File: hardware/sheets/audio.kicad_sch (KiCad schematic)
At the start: 17 parts, among them J2 LineOut_TRS, U1 MCP6002

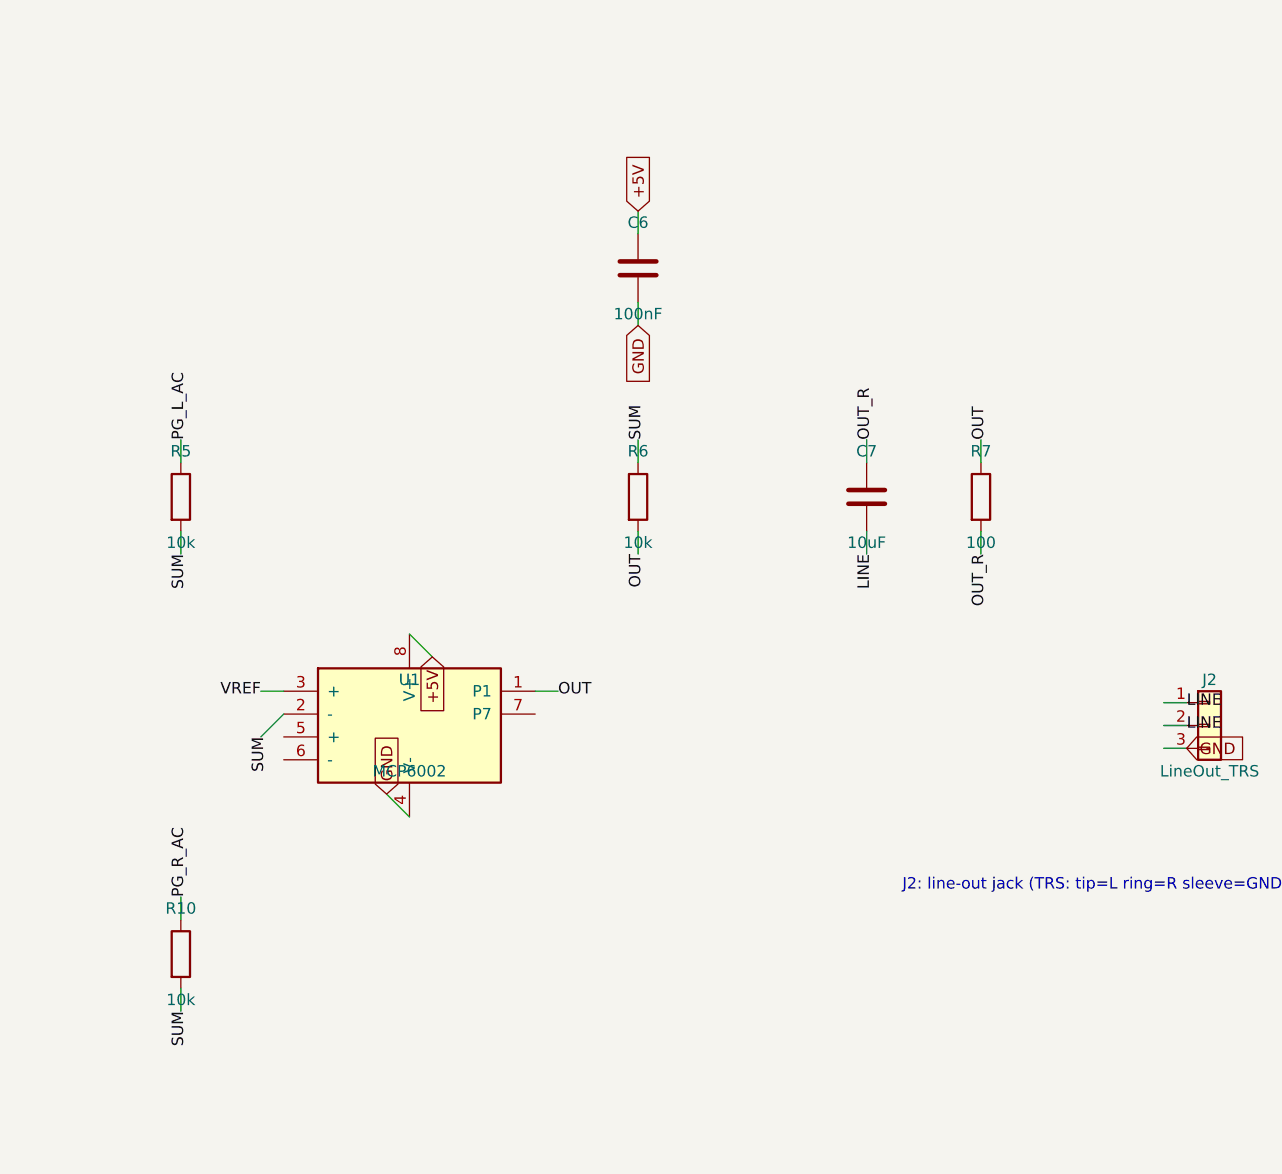
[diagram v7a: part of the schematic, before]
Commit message: Design-review fixes: reset parking, IRQ8 off the header, analog cleanups
Netlist-wide review sweep. IRQ8 leaves the 60-pin ISA header (pin 15 is a
second GND return; the on-board RTC owns IRQ8 exclusively, so its push-pull
drive is now correct by construction). Bus MCU Hi-Z parking completed:
~CPURESET pulled low (V20 held in reset while the MCU is unprogrammed),
~DACK1/~REFRESH parked deasserted, DRQ1 idled low. Supervisor 12 MHz crystal
damping R actually in series now (was parallel-to-nothing), plus a second
USBLC6 so both prog-port SW2 positions are ESD-protected. Audio: 0.5x PG
summing (MCP6002 headroom), 100k LINE bleed, unit B parked as a follower --
and the SUM stub moved off pin 5's row, where wiring unit B would have
silently merged SUM into VREF. CH224K VDD fed through 1k per the WCH ref
design. VGA blue ladder rescaled 1k/510 -> 820/470 (was ~12% blue-deficient).
Spare CMOS gate inputs grounded uniformly (cpu_core/rtc/storage); UART_RXD
pulled up (SIN idles at mark with JP1 open); dead pins/parts dropped
(com_port CLK, parallel RESET_DRV, storage R3). Bus CLK fixed at 7.16 MHz
logged as a decision. New passives mapped to JLC basic parts in parts.py.

Co-Authored-By: Claude Fable 5 <noreply@anthropic.com>
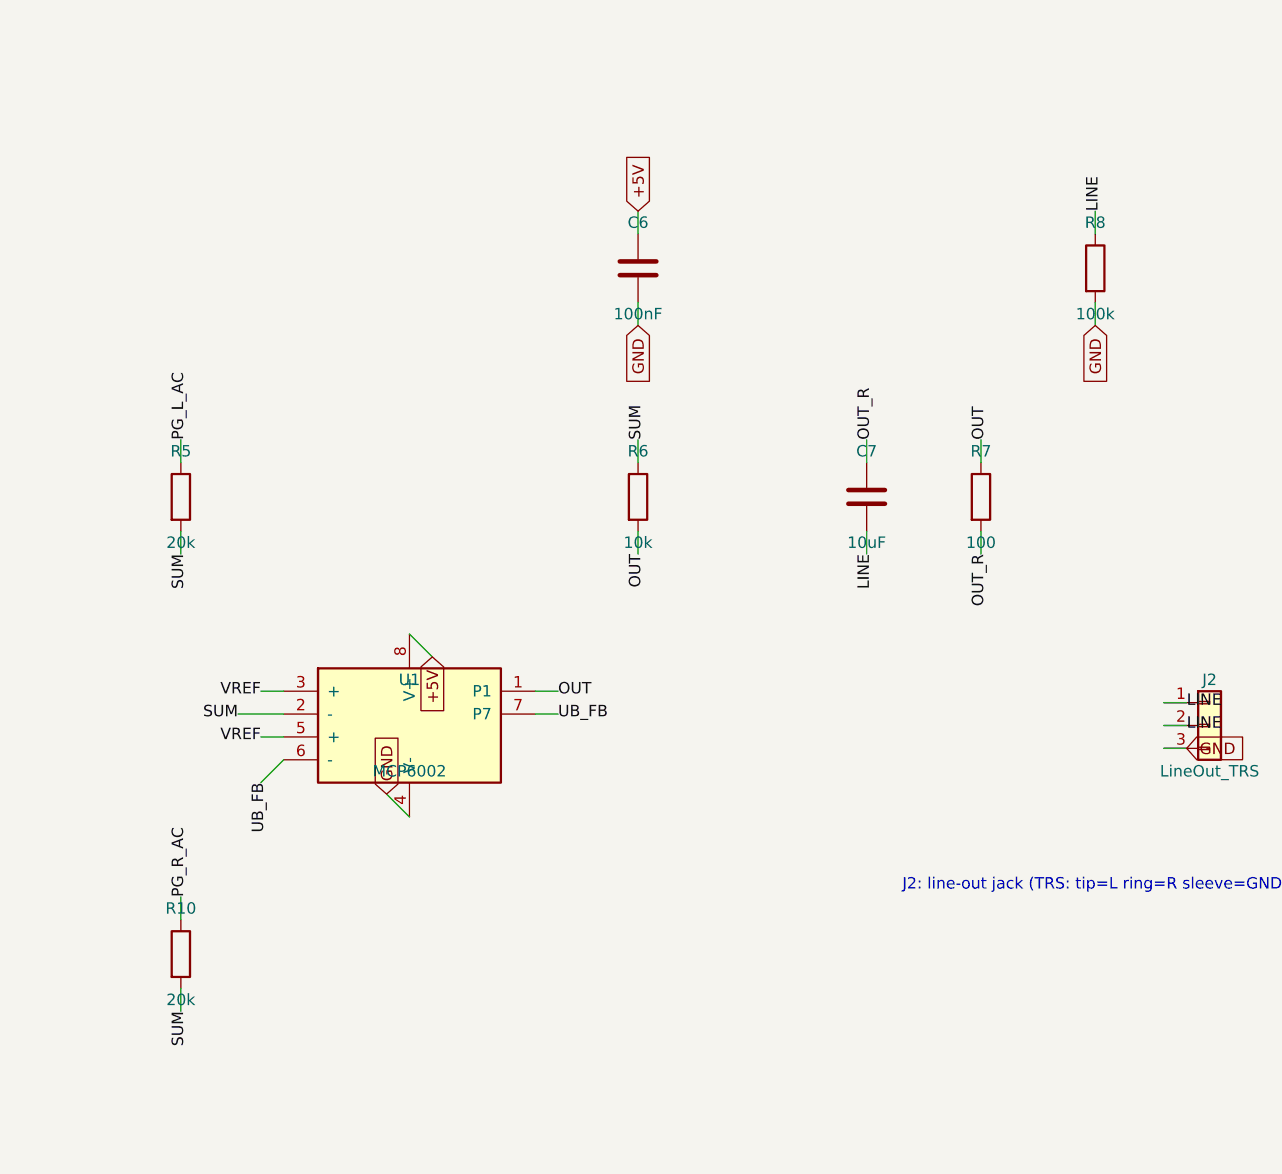
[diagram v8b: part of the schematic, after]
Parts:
- added J2: LineOut_TRS, symbol Connector_Generic:Conn_01x03
- R10, R5: value 10k -> 20k; LCSC Part Num C25804 -> C4184
- R8: renamed from J2; value LineOut_TRS -> 100k; symbol Connector_Generic:Conn_01x03 -> Device:R; LCSC Part Num C2337 -> C25803
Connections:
- net GND: now also R8.2, J2.3 (Pin_3); no longer R8.3 (Pin_3)
- net LINE: now also J2.1 (Pin_1), J2.2 (Pin_2); no longer R8.2 (Pin_2)
- net VREF: now also U1.5 (+)
- net UB_FB: now reaches U1.6 (-)
- net UB_FB: now also U1.7 (P7)
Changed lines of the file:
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@@
 		(pts
 			(xy 163.83 151.13)
-			(xy 161.29 153.67)
+			(xy 158.75 151.13)
 		)
 		(stroke
@@
 	)
 	(label "SUM"
-		(at 161.29 153.67 270)
+		(at 158.75 151.13 180)
 		(effects
 			(font
@@
 	(label "LINE"
 		(at 228.6 133.35 270)
+		(effects
+			(font
+				(size 1.27 1.27)
+			)
+		)
+	)
+	(wire
+		(pts
+			(xy 254 97.79)
+			(xy 254 95.25)
+		)
+		(stroke
+			(width 0)
+			(type default)
+		)
+	)
+	(label "LINE"
+		(at 254 95.25 90)
+		(effects
+			(font
+				(size 1.27 1.27)
+			)
+		)
+	)
+	(wire
+		(pts
+			(xy 254 105.41)
+			(xy 254 107.95)
+		)
+		(stroke
+			(width 0)
+			(type default)
+		)
+	)
+	(global_label "GND"
+		(shape input)
+		(at 254 107.95 270)
+		(effects
+			(font
+				(size 1.27 1.27)
+			)
+		)
+	)
+	(wire
+		(pts
+			(xy 163.83 153.67)
+			(xy 161.29 153.67)
+		)
+		(stroke
+			(width 0)
+			(type default)
+		)
+	)
+	(label "VREF"
+		(at 161.29 153.67 180)
+		(effects
+			(font
+				(size 1.27 1.27)
+			)
+		)
+	)
+	(wire
+		(pts
+			(xy 163.83 156.21)
+			(xy 161.29 158.75)
+		)
+		(stroke
+			(width 0)
+			(type default)
+		)
+	)
+	(label "UB_FB"
+		(at 161.29 158.75 270)
+		(effects
+			(font
+				(size 1.27 1.27)
+			)
+		)
+	)
+	(wire
+		(pts
+			(xy 191.77 151.13)
+			(xy 194.31 151.13)
+		)
+		(stroke
+			(width 0)
+			(type default)
+		)
+	)
+	(label "UB_FB"
+		(at 194.31 151.13 0)
 		(effects
 			(font
@@
 		(instances
 			(project "mini-xt"
-				(path "/26736c46-8b40-5460-874f-03596d17270c/3608bfd0-7703-513a-bc2e-2c197268d7ed"
+				(path "/26736c46-8b40-5460-874f-03596d17270c/4d185cde-1239-5609-9fdc-bfd3b5da75e8"
 					(reference "R1101")
 					(unit 1)
@@
 		(instances
 			(project "mini-xt"
-				(path "/26736c46-8b40-5460-874f-03596d17270c/3608bfd0-7703-513a-bc2e-2c197268d7ed"
+				(path "/26736c46-8b40-5460-874f-03596d17270c/4d185cde-1239-5609-9fdc-bfd3b5da75e8"
 					(reference "R1102")
 					(unit 1)
@@
 		(instances
 			(project "mini-xt"
-				(path "/26736c46-8b40-5460-874f-03596d17270c/3608bfd0-7703-513a-bc2e-2c197268d7ed"
+				(path "/26736c46-8b40-5460-874f-03596d17270c/4d185cde-1239-5609-9fdc-bfd3b5da75e8"
 					(reference "C1101")
 					(unit 1)
@@
 		(instances
 			(project "mini-xt"
-				(path "/26736c46-8b40-5460-874f-03596d17270c/3608bfd0-7703-513a-bc2e-2c197268d7ed"
+				(path "/26736c46-8b40-5460-874f-03596d17270c/4d185cde-1239-5609-9fdc-bfd3b5da75e8"
 					(reference "R1103")
 					(unit 1)
@@
 		(instances
 			(project "mini-xt"
-				(path "/26736c46-8b40-5460-874f-03596d17270c/3608bfd0-7703-513a-bc2e-2c197268d7ed"
+				(path "/26736c46-8b40-5460-874f-03596d17270c/4d185cde-1239-5609-9fdc-bfd3b5da75e8"
 					(reference "C1102")
 					(unit 1)
@@
 		(instances
 			(project "mini-xt"
-				(path "/26736c46-8b40-5460-874f-03596d17270c/3608bfd0-7703-513a-bc2e-2c197268d7ed"
+				(path "/26736c46-8b40-5460-874f-03596d17270c/4d185cde-1239-5609-9fdc-bfd3b5da75e8"
 					(reference "C1103")
 					(unit 1)
@@
 		(instances
 			(project "mini-xt"
-				(path "/26736c46-8b40-5460-874f-03596d17270c/3608bfd0-7703-513a-bc2e-2c197268d7ed"
+				(path "/26736c46-8b40-5460-874f-03596d17270c/4d185cde-1239-5609-9fdc-bfd3b5da75e8"
 					(reference "C1104")
 					(unit 1)
@@
 		(instances
 			(project "mini-xt"
-				(path "/26736c46-8b40-5460-874f-03596d17270c/3608bfd0-7703-513a-bc2e-2c197268d7ed"
+				(path "/26736c46-8b40-5460-874f-03596d17270c/4d185cde-1239-5609-9fdc-bfd3b5da75e8"
 					(reference "C1105")
 					(unit 1)
@@
 		(instances
 			(project "mini-xt"
-				(path "/26736c46-8b40-5460-874f-03596d17270c/3608bfd0-7703-513a-bc2e-2c197268d7ed"
+				(path "/26736c46-8b40-5460-874f-03596d17270c/4d185cde-1239-5609-9fdc-bfd3b5da75e8"
 					(reference "U1101")
 					(unit 1)
@@
 		(instances
 			(project "mini-xt"
-				(path "/26736c46-8b40-5460-874f-03596d17270c/3608bfd0-7703-513a-bc2e-2c197268d7ed"
+				(path "/26736c46-8b40-5460-874f-03596d17270c/4d185cde-1239-5609-9fdc-bfd3b5da75e8"
 					(reference "C1106")
 					(unit 1)
@@
 		(instances
 			(project "mini-xt"
-				(path "/26736c46-8b40-5460-874f-03596d17270c/3608bfd0-7703-513a-bc2e-2c197268d7ed"
+				(path "/26736c46-8b40-5460-874f-03596d17270c/4d185cde-1239-5609-9fdc-bfd3b5da75e8"
 					(reference "R1104")
 					(unit 1)
@@
 			)
 		)
-		(property "Value" "10k"
+		(property "Value" "20k"
 			(at 152.4 132.08 0)
 			(effects
@@
 			)
 		)
-		(property "LCSC Part Num" "C25804"
+		(property "LCSC Part Num" "C4184"
 			(at 152.4 127 0)
 			(effects
@@
 		(instances
 			(project "mini-xt"
-				(path "/26736c46-8b40-5460-874f-03596d17270c/3608bfd0-7703-513a-bc2e-2c197268d7ed"
+				(path "/26736c46-8b40-5460-874f-03596d17270c/4d185cde-1239-5609-9fdc-bfd3b5da75e8"
 					(reference "R1105")
 					(unit 1)
@@
 			)
 		)
-		(property "Value" "10k"
+		(property "Value" "20k"
 			(at 152.4 182.88 0)
 			(effects
@@
 			)
 		)
-		(property "LCSC Part Num" "C25804"
+		(property "LCSC Part Num" "C4184"
 			(at 152.4 177.8 0)
 			(effects
@@
 		(instances
 			(project "mini-xt"
-				(path "/26736c46-8b40-5460-874f-03596d17270c/3608bfd0-7703-513a-bc2e-2c197268d7ed"
+				(path "/26736c46-8b40-5460-874f-03596d17270c/4d185cde-1239-5609-9fdc-bfd3b5da75e8"
 					(reference "R1110")
 					(unit 1)
@@
 		(instances
 			(project "mini-xt"
-				(path "/26736c46-8b40-5460-874f-03596d17270c/3608bfd0-7703-513a-bc2e-2c197268d7ed"
+				(path "/26736c46-8b40-5460-874f-03596d17270c/4d185cde-1239-5609-9fdc-bfd3b5da75e8"
 					(reference "R1106")
 					(unit 1)
@@
 		(instances
 			(project "mini-xt"
-				(path "/26736c46-8b40-5460-874f-03596d17270c/3608bfd0-7703-513a-bc2e-2c197268d7ed"
+				(path "/26736c46-8b40-5460-874f-03596d17270c/4d185cde-1239-5609-9fdc-bfd3b5da75e8"
 					(reference "R1107")
 					(unit 1)
@@
 		(instances
 			(project "mini-xt"
-				(path "/26736c46-8b40-5460-874f-03596d17270c/3608bfd0-7703-513a-bc2e-2c197268d7ed"
+				(path "/26736c46-8b40-5460-874f-03596d17270c/4d185cde-1239-5609-9fdc-bfd3b5da75e8"
 					(reference "C1107")
+					(unit 1)
+				)
+			)
+		)
+	)
+	(symbol
+		(lib_id "Device:R")
+		(at 254 101.6 0)
+		(unit 1)
+		(exclude_from_sim no)
+		(in_bom yes)
+		(on_board yes)
+		(dnp no)
+		(fields_autoplaced yes)
+		(property "Reference" "R8"
+			(at 254 96.52 0)
+			(effects
+				(font
+					(size 1.27 1.27)
+				)
+			)
+		)
+		(property "Value" "100k"
+			(at 254 106.68 0)
+			(effects
+				(font
+					(size 1.27 1.27)
+				)
+			)
+		)
+		(property "Footprint" ""
+			(at 254 101.6 0)
+			(effects
+				(font
+					(size 1.27 1.27)
+				)
+				(hide yes)
+			)
+		)
+		(property "LCSC Part Num" "C25803"
+			(at 254 101.6 0)
+			(effects
+				(font
+					(size 1.27 1.27)
+				)
+				(hide yes)
+			)
+		)
+		(pin "1"
+		)
+		(pin "2"
+		)
+		(instances
+			(project "mini-xt"
+				(path "/26736c46-8b40-5460-874f-03596d17270c/4d185cde-1239-5609-9fdc-bfd3b5da75e8"
+					(reference "R1108")
 					(unit 1)
 				)
@@
 		(instances
 			(project "mini-xt"
-				(path "/26736c46-8b40-5460-874f-03596d17270c/3608bfd0-7703-513a-bc2e-2c197268d7ed"
+				(path "/26736c46-8b40-5460-874f-03596d17270c/4d185cde-1239-5609-9fdc-bfd3b5da75e8"
 					(reference "J1102")
 					(unit 1)
